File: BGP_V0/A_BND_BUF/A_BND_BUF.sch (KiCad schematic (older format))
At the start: 27 parts, among them P1 CONN_01X02, P2 CONN_01X02, P3 CONN_01X04, Q1 2SK208, Q2 2SK208, U1 OPA180

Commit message: Gerbers
Mainly getting gerbers ready.  Issue with pots overlapping other boards in silk screens - top and bottom.
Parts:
- removed P3: CONN_01X04, Connectors_Molex:Molex_MicroLatch-53253-0470_04x2.00mm_Straight, symbol CONN_01X04
- added P?: Conn_01x05, symbol Conn_01x05
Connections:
- net Earth: now also D1.1 (K), D2.1 (K), P?.3 (Pin_3); no longer D1.2 (A), D2.2 (A)
- net OUT: now also P?.2 (Pin_2)
- net REF: now also P?.1 (Pin_1)
- net V+: now also P?.4 (Pin_4)
- net at Q1.1 (S), R5.2: now also D1.2 (A); no longer D1.1 (K)
- net at Q2.1 (S), R6.2: now also D2.2 (A); no longer D2.1 (K)
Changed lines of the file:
@@
 F 3 "" H 5200 3400 50  0000 C CNN
 	1    5200 3400
-	0    1    1    0
-$EndComp
-$Comp
-L CONN_01X04 P3
-U 1 1 5A2750D7
-P 7050 4450
-F 0 "P3" H 7050 4700 50  0000 C CNN
-F 1 "CONN_01X04" V 7150 4450 50  0000 C CNN
-F 2 "Connectors_Molex:Molex_MicroLatch-53253-0470_04x2.00mm_Straight" H 7050 4450 50  0001 C CNN
-F 3 "" H 7050 4450 50  0000 C CNN
-	1    7050 4450
-	-1   0    0    1
+	0    -1   -1   0
 $EndComp
 Text Label 7250 4300 0    60   ~ 0
@@
 F 3 "" H 5200 4500 50  0000 C CNN
 	1    5200 4500
-	0    1    1    0
+	0    -1   -1   0
 $EndComp
 $Comp
@@
 REF
 $Comp
-L Earth #PWR06
+L Earth #PWR05
 U 1 1 5A27A98F
 P 5200 4650
-F 0 "#PWR06" H 5200 4400 50  0001 C CNN
+F 0 "#PWR05" H 5200 4400 50  0001 C CNN
 F 1 "Earth" H 5200 4500 50  0001 C CNN
 F 2 "" H 5200 4650 50  0000 C CNN
@@
 $EndComp
 $Comp
-L Earth #PWR07
+L Earth #PWR06
 U 1 1 5A27AB22
 P 5200 3550
-F 0 "#PWR07" H 5200 3300 50  0001 C CNN
+F 0 "#PWR06" H 5200 3300 50  0001 C CNN
 F 1 "Earth" H 5200 3400 50  0001 C CNN
 F 2 "" H 5200 3550 50  0000 C CNN
@@
 $EndComp
 $Comp
-L Earth #PWR08
+L Earth #PWR07
 U 1 1 5A2862BB
 P 7700 4550
-F 0 "#PWR08" H 7700 4300 50  0001 C CNN
+F 0 "#PWR07" H 7700 4300 50  0001 C CNN
 F 1 "Earth" H 7700 4400 50  0001 C CNN
 F 2 "" H 7700 4550 50  0000 C CNN
@@
 Text Label 7700 3800 3    60   ~ 0
 REF
+$Comp
+L Conn_01x05 P?
+U 1 1 5A5738D7
+P 7050 4400
+F 0 "P?" H 7050 4700 50  0000 C CNN
+F 1 "Conn_01x05" H 7050 4100 50  0000 C CNN
+F 2 "" H 7050 4400 50  0001 C CNN
+F 3 "" H 7050 4400 50  0001 C CNN
+	1    7050 4400
+	-1   0    0    1
+$EndComp
 $EndSCHEMATC

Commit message: Pot fixups for silkscreen overlap
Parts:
- P3: renamed from P?; footprint (none) -> Connectors_Molex:Molex_MicroLatch-53253-0570_05x2.00mm_Straight
- RV1: footprint Potentiometers:Potentiometer_Alps_RK097_Double_Vertical -> LIBS:Potentiometer_Alps_RK097_Double_Vertical
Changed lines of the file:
@@
 F 0 "RV1" H 6210 3910 50  0000 C CNN
 F 1 "RK0971210Z2M" H 6400 3300 50  0000 C CNN
-F 2 "Potentiometers:Potentiometer_Alps_RK097_Double_Vertical" H 6050 3600 50  0001 C CNN
+F 2 "LIBS:Potentiometer_Alps_RK097_Double_Vertical" H 6050 3600 50  0001 C CNN
 F 3 "" H 6050 3600 50  0000 C CNN
 	1    6050 3600
@@
 REF
 $Comp
-L Conn_01x05 P?
+L Conn_01x05 P3
 U 1 1 5A5738D7
 P 7050 4400
-F 0 "P?" H 7050 4700 50  0000 C CNN
+F 0 "P3" H 7050 4700 50  0000 C CNN
 F 1 "Conn_01x05" H 7050 4100 50  0000 C CNN
-F 2 "" H 7050 4400 50  0001 C CNN
+F 2 "Connectors_Molex:Molex_MicroLatch-53253-0570_05x2.00mm_Straight" H 7050 4400 50  0001 C CNN
 F 3 "" H 7050 4400 50  0001 C CNN
 	1    7050 4400

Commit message: V_0 Updates for caps, gerbers updated
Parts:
- C1, C2: footprint Capacitors_SMD:C_1210_HandSoldering -> Capacitors_Tantalum_SMD:TantalC_SizeR_EIA-2012
- C3, C4, C5: footprint Capacitors_SMD:C_1206_HandSoldering -> Capacitors_Tantalum_SMD:TantalC_SizeS_EIA-3216
- C6: footprint Capacitors_Tantalum_SMD:TantalC_SizeB_EIA-3528_HandSoldering -> Capacitors_SMD:C_0805_HandSoldering
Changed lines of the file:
@@
 F 0 "C1" H 4560 3120 50  0000 L CNN
 F 1 "0.1u" H 4560 2970 50  0000 L CNN
-F 2 "Capacitors_SMD:C_1210_HandSoldering" H 4550 3050 50  0001 C CNN
+F 2 "Capacitors_Tantalum_SMD:TantalC_SizeR_EIA-2012" H 4550 3050 50  0001 C CNN
 F 3 "" H 4550 3050 50  0000 C CNN
 	1    4550 3050
@@
 F 0 "C3" H 5760 3370 50  0000 L CNN
 F 1 "10u" H 5760 3220 50  0000 L CNN
-F 2 "Capacitors_SMD:C_1206_HandSoldering" H 5750 3300 50  0001 C CNN
+F 2 "Capacitors_Tantalum_SMD:TantalC_SizeS_EIA-3216" H 5750 3300 50  0001 C CNN
 F 3 "" H 5750 3300 50  0000 C CNN
 	1    5750 3300
@@
 F 0 "C2" H 4560 4220 50  0000 L CNN
 F 1 "0.1u" H 4560 4070 50  0000 L CNN
-F 2 "Capacitors_SMD:C_1210_HandSoldering" H 4550 4150 50  0001 C CNN
+F 2 "Capacitors_Tantalum_SMD:TantalC_SizeR_EIA-2012" H 4550 4150 50  0001 C CNN
 F 3 "" H 4550 4150 50  0000 C CNN
 	1    4550 4150
@@
 F 0 "C4" H 5760 4470 50  0000 L CNN
 F 1 "10u" H 5760 4320 50  0000 L CNN
-F 2 "Capacitors_SMD:C_1206_HandSoldering" H 5750 4400 50  0001 C CNN
+F 2 "Capacitors_Tantalum_SMD:TantalC_SizeS_EIA-3216" H 5750 4400 50  0001 C CNN
 F 3 "" H 5750 4400 50  0000 C CNN
 	1    5750 4400
@@
 F 0 "C5" H 7560 3570 50  0000 L CNN
 F 1 "10u" H 7560 3420 50  0000 L CNN
-F 2 "Capacitors_SMD:C_1206_HandSoldering" H 7550 3500 50  0001 C CNN
+F 2 "Capacitors_Tantalum_SMD:TantalC_SizeS_EIA-3216" H 7550 3500 50  0001 C CNN
 F 3 "" H 7550 3500 50  0000 C CNN
 	1    7550 3500
@@
 F 0 "C6" H 7710 4520 50  0000 L CNN
 F 1 "22u" H 7710 4370 50  0000 L CNN
-F 2 "Capacitors_Tantalum_SMD:TantalC_SizeB_EIA-3528_HandSoldering" H 7700 4450 50  0001 C CNN
+F 2 "Capacitors_SMD:C_0805_HandSoldering" H 7700 4450 50  0001 C CNN
 F 3 "" H 7700 4450 50  0000 C CNN
 	1    7700 4450

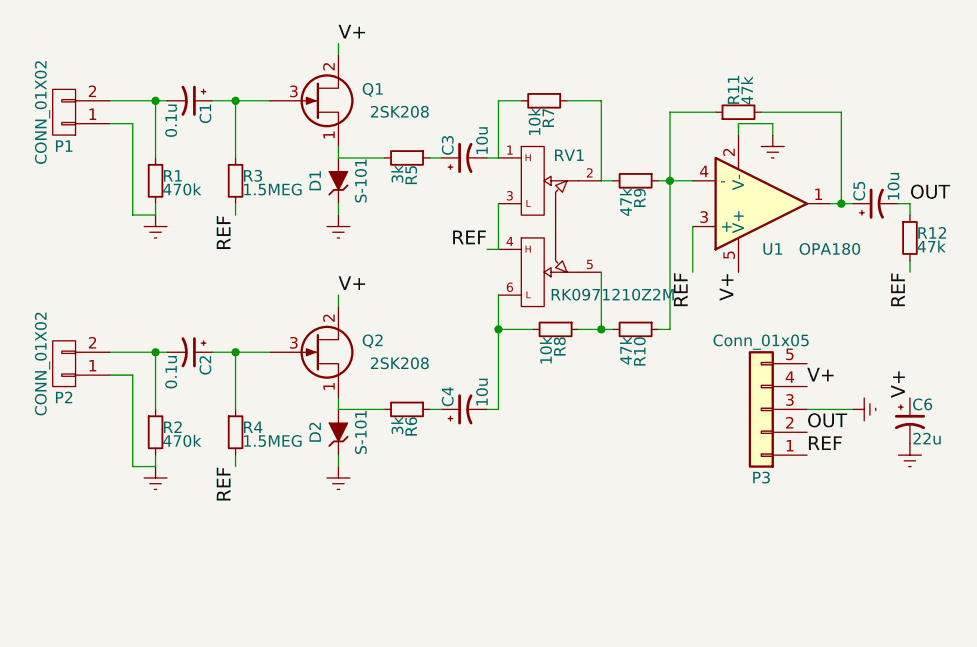
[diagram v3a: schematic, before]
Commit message: V0 BUF and BT Edits
V0 Buffer change from CRD to JFET CCS. BT stack changed to reflect +/- 9V changes.
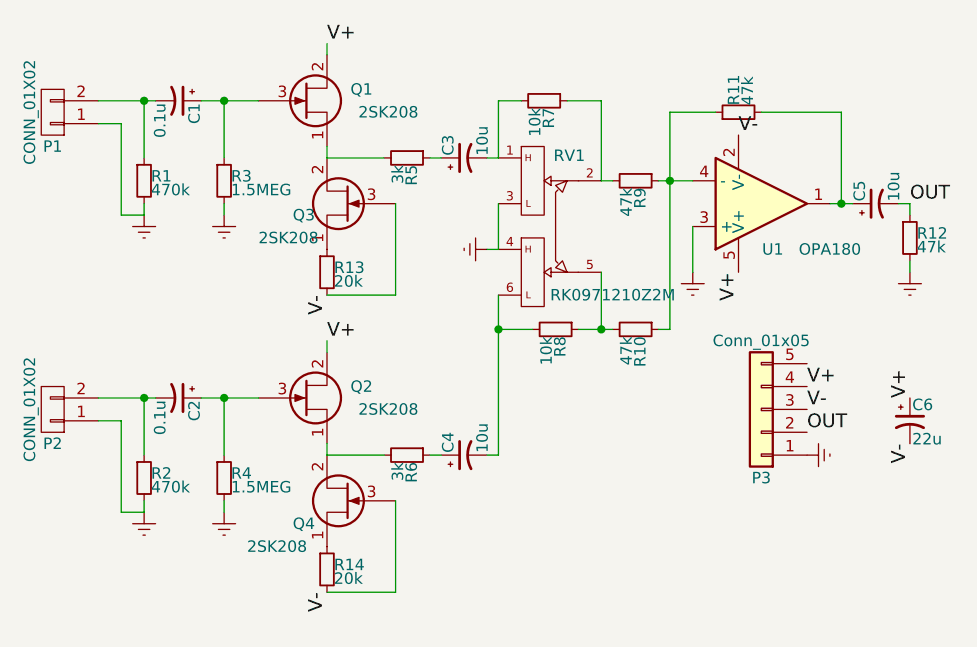
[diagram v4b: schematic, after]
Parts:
- removed D1, D2: S-101, Diodes_SMD:SOD-123, symbol ZENERsmall
- added Q3, Q4: 2SK208, TO_SOT_Packages_SMD:SC-59_Handsoldering, symbol Q_NJFET_SDG
- added R13, R14: 20k, Resistors_SMD:R_0603_HandSoldering, symbol R_Small
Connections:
- net REF is gone; now on net Earth: P3.1 (Pin_1), R12.2, R3.2, R4.2, RV1.3, RV1.4, U1.3 (+)
- net Earth: no longer C6.2, P3.3 (Pin_3), U1.2 (V-)
- net at Q1.1 (S), R5.2: now also Q3.2 (D)
- net at Q2.1 (S), R6.2: now also Q4.2 (D)
- new net: Q3.1 (S), R13.1
- new net: Q4.1 (S), R14.1
- new net V-: C6.2, P3.3 (Pin_3), Q3.3 (G), Q4.3 (G), R13.2, R14.2, U1.2 (V-)
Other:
- moved on the sheet: C1, C2, C4, P1, P2, Q1, Q2, R1, R2, R3, R4, R6
